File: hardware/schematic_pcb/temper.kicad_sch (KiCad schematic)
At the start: 56 parts, among them J1 conn_01x03, J2 conn_01x03, J3 conn_01x03, J4 conn_01x03, J5 Charge Connector, J6 MCU Serial I/F, J7 Conn_01x10, M1 AO3401A, Q1 2N7002, Q2 2N7002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

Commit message: /TON changed to TON for latest SCHEMATIC/PCB
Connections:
- net /TON renamed TON
- no-connect marks 16 -> 15
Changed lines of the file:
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@@
-	)
-	(no_connect
-		(at 167.64 -29.21)
 	)
 	(no_connect
@@
 		)
 	)
-	(label "{slash}TON"
+	(label "TON"
 		(at 129.54 148.59 0)
 		(effects
@@
 		)
 	)
-	(label "{slash}TON"
+	(label "TON"
 		(at 113.03 64.77 0)
 		(effects

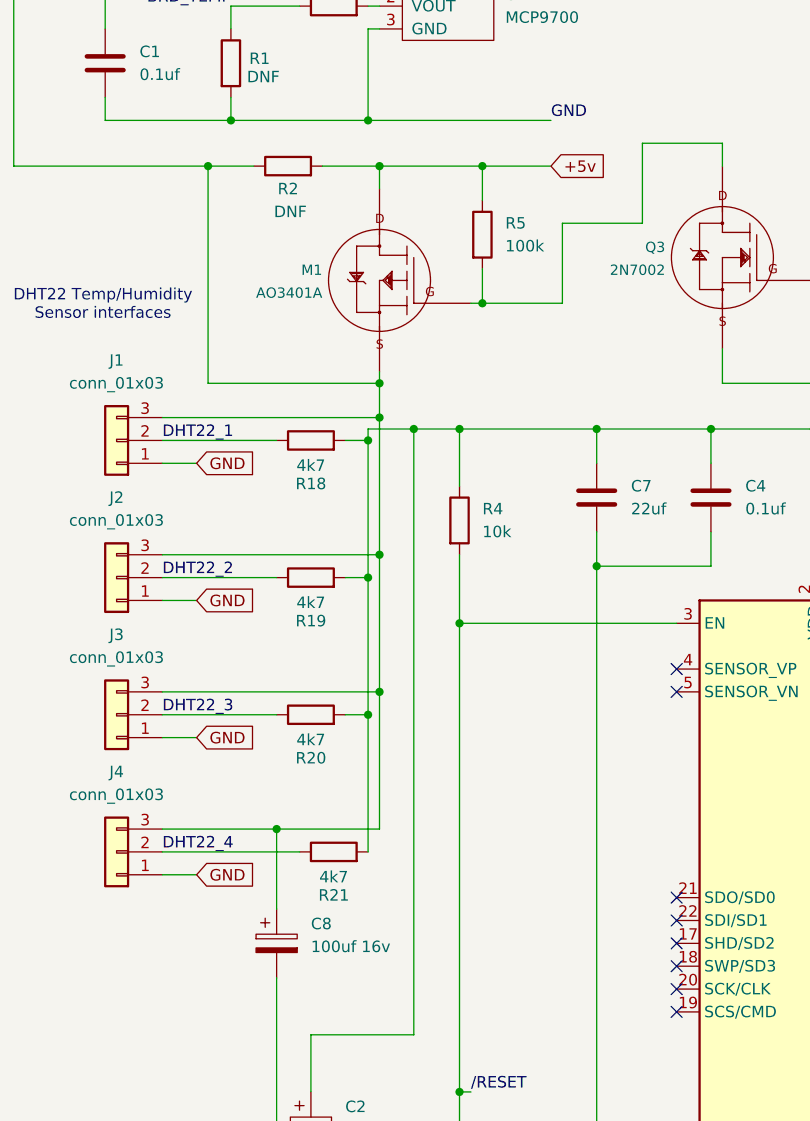
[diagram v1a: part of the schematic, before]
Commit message: - Fix incorrect M1 connectivity. - Bump PCB to V2.0
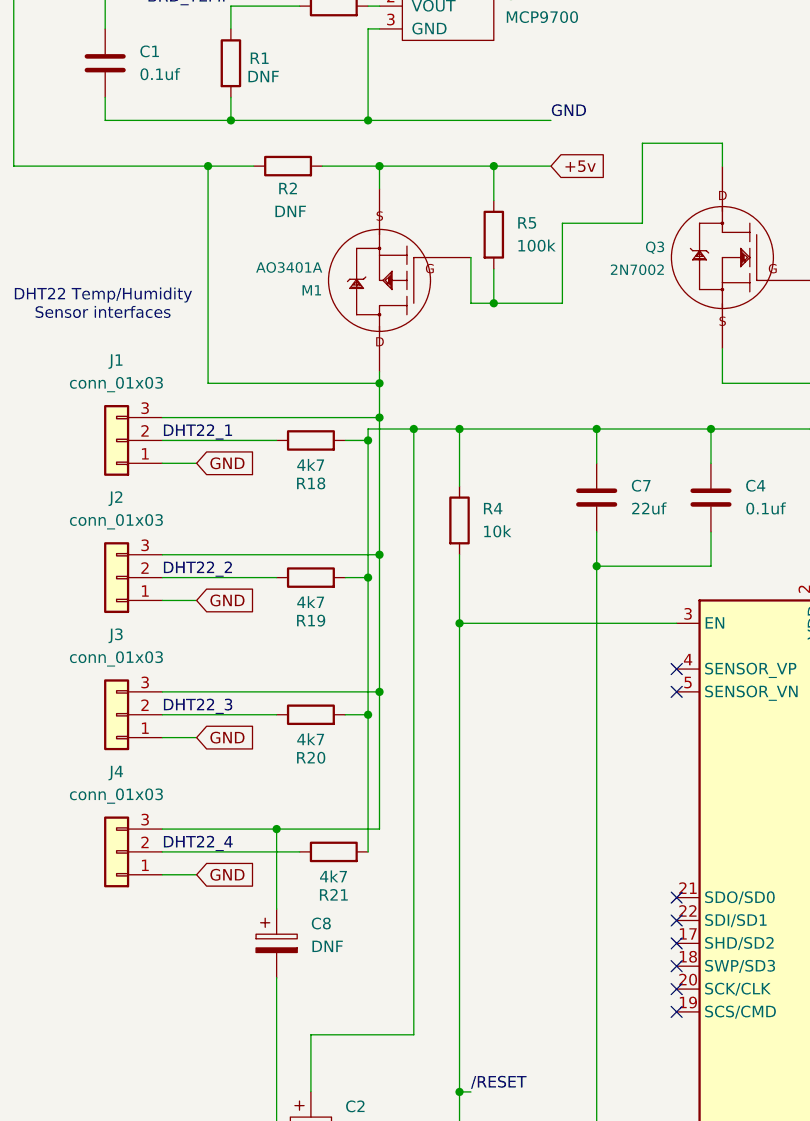
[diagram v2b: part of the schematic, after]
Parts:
- C8: value 100uf 16v -> DNF
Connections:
- net +5v: now also M1.2 (S1); no longer M1.3 (D1)
- net at C1.1, C8.1, J1.3 (Pin_3)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: now also M1.3 (D1); no longer M1.2 (S1)
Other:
- moved on the sheet: M1, R5
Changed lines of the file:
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@@
 	(paper "A4")
 	(title_block
-		(date "2026-05-14")
-		(rev "1.9")
+		(date "2026-06-03")
+		(rev "12.0")
 		(comment 1 "1.8 - 1.9 no changes to schematic. C2 moved on PCB.")
 	)
@@
 	)
 	(junction
-		(at 73.66 52.07)
+		(at 43.18 52.07)
 		(diameter 0)
 		(color 0 0 0 0)
 	)
 	(junction
-		(at 43.18 52.07)
+		(at 71.12 102.87)
 		(diameter 0)
 		(color 0 0 0 0)
 	)
 	(junction
-		(at 71.12 102.87)
+		(at 50.8 182.88)
 		(diameter 0)
 		(color 0 0 0 0)
 	)
 	(junction
-		(at 50.8 182.88)
+		(at 74.93 52.07)
 		(diameter 0)
 		(color 0 0 0 0)
@@
 	)
 	(junction
-		(at 73.66 67.31)
-		(diameter 0)
-		(color 0 0 0 0)
-	)
-	(junction
 		(at 234.95 90.17)
 		(diameter 0)
@@
 	)
 	(junction
+		(at 74.93 67.31)
+		(diameter 0)
+		(color 0 0 0 0)
+	)
+	(junction
 		(at 200.66 53.34)
 		(diameter 0)
@@
 	(wire
 		(pts
+			(xy 74.93 67.31) (xy 82.55 67.31)
+		)
+		(stroke
+			(width 0)
+			(type default)
+		)
+	)
+	(wire
+		(pts
 			(xy 110.49 168.91) (xy 110.49 182.88)
 		)
@@
 	(wire
 		(pts
-			(xy 73.66 67.31) (xy 82.55 67.31)
-		)
-		(stroke
-			(width 0)
-			(type default)
-		)
-	)
-	(wire
-		(pts
 			(xy 180.34 86.36) (xy 180.34 90.17)
 		)
@@
 	(wire
 		(pts
-			(xy 81.28 52.07) (xy 73.66 52.07)
+			(xy 81.28 52.07) (xy 74.93 52.07)
 		)
 		(stroke
@@
 	(wire
 		(pts
-			(xy 73.66 67.31) (xy 73.66 63.5)
+			(xy 74.93 67.31) (xy 74.93 63.5)
 		)
 		(stroke
@@
 	(wire
 		(pts
-			(xy 73.66 52.07) (xy 62.23 52.07)
+			(xy 62.23 52.07) (xy 74.93 52.07)
 		)
 		(stroke
@@
 	(wire
 		(pts
-			(xy 73.66 52.07) (xy 73.66 55.88)
+			(xy 74.93 52.07) (xy 74.93 55.88)
 		)
 		(stroke
@@
 	(wire
 		(pts
-			(xy 72.39 67.31) (xy 73.66 67.31)
+			(xy 72.39 67.31) (xy 74.93 67.31)
 		)
 		(stroke
@@
 	(wire
 		(pts
+			(xy 72.39 62.23) (xy 72.39 67.31)
+		)
+		(stroke
+			(width 0)
+			(type default)
+		)
+	)
+	(wire
+		(pts
 			(xy 194.31 107.95) (xy 194.31 109.22)
 		)
@@
 			)
 		)
-		(property "Value" "100uf 16v"
+		(property "Value" "DNF"
 			(at 54.61 138.8109 0)
 			(show_name no)
@@
 	(symbol
 		(lib_id "pja_1:DMP3099L-7")
-		(at 62.23 64.77 0)
-		(mirror y)
+		(at 62.23 64.77 180)
 		(unit 1)
 		(body_style 1)
@@
 		(dnp no)
 		(property "Reference" "M1"
-			(at 55.88 63.627 0)
+			(at 55.88 65.913 0)
 			(show_name no)
 			(do_not_autoplace no)
@@
 		)
 		(property "Value" "AO3401A"
-			(at 55.88 66.167 0)
+			(at 55.88 63.373 0)
 			(show_name no)
 			(do_not_autoplace no)
@@
 		)
 		(property "Footprint" "Package_TO_SOT_SMD:SOT-23-3"
-			(at 61.468 60.96 0)
+			(at 61.468 68.58 0)
 			(hide yes)
 			(show_name no)
@@
 	(symbol
 		(lib_id "Device:R")
-		(at 73.66 59.69 0)
+		(at 74.93 59.69 0)
 		(unit 1)
 		(body_style 1)
@@
 		(fields_autoplaced yes)
 		(property "Reference" "R5"
-			(at 76.2 58.4199 0)
+			(at 77.47 58.4199 0)
 			(show_name no)
 			(do_not_autoplace no)
@@
 		)
 		(property "Value" "100k"
-			(at 76.2 60.9599 0)
+			(at 77.47 60.9599 0)
 			(show_name no)
 			(do_not_autoplace no)
@@
 		)
 		(property "Footprint" "Resistor_SMD:R_0402_1005Metric_Pad0.72x0.64mm_HandSolder"
-			(at 71.882 59.69 90)
+			(at 73.152 59.69 90)
 			(hide yes)
 			(show_name no)
@@
 		)
 		(property "Datasheet" ""
-			(at 73.66 59.69 0)
+			(at 74.93 59.69 0)
 			(hide yes)
 			(show_name no)
@@
 		)
 		(property "Description" "Resistor"
-			(at 73.66 59.69 0)
+			(at 74.93 59.69 0)
 			(hide yes)
 			(show_name no)
@@
 		)
 		(property "LCSC" "C25741"
-			(at 73.66 59.69 0)
+			(at 74.93 59.69 0)
 			(hide yes)
 			(show_name no)
